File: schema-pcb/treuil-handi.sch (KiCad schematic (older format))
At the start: 7 parts, among them K1 PPM, SW1 calibration, U2 AS5048B Pot, U3 AS5048B moteur

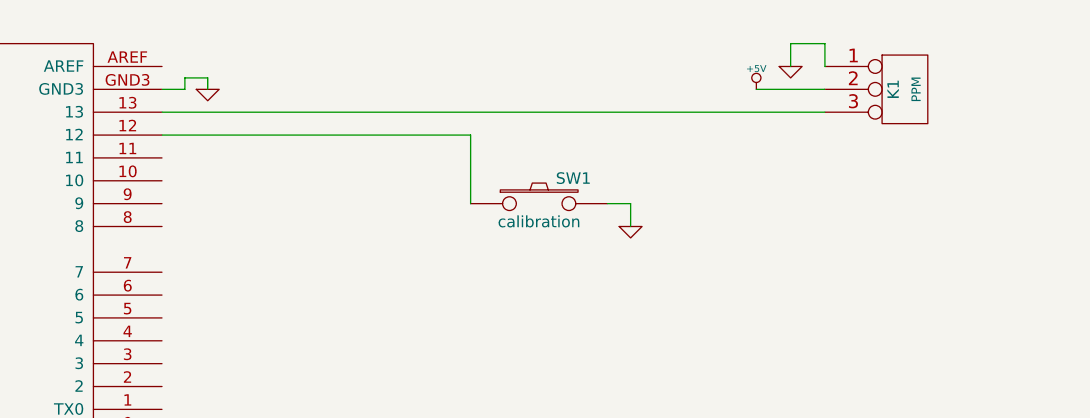
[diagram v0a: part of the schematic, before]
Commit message: maj du schema, doc I2C
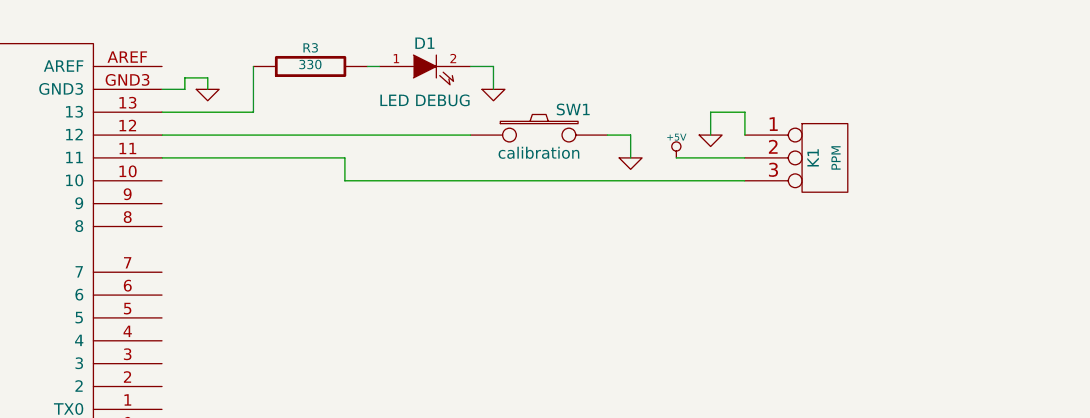
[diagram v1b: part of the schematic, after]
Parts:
- added D1: LED DEBUG, ~, symbol LED
- added R3: 330, ~, symbol R
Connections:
- net GND: now also D1.2 (K)
- net at SHIELD1.11: now also K1.3 (P3)
- net at SHIELD1.13: now also R3.1; no longer K1.3 (P3)
- new net: D1.1 (A), R3.2
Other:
- moved on the sheet: K1, SW1
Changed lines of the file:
@@
-EESchema Schematic File Version 2  date 03/07/2014 16:32:03
+EESchema Schematic File Version 2  date 02/08/2014 10:49:15
 LIBS:power
 LIBS:device
@@
 Sheet 1 1
 Title ""
-Date "3 jul 2014"
+Date "2 aug 2014"
 Rev ""
 Comp ""
@@
 L SW_PUSH SW1
 U 1 1 53B1346F
-P 5200 1900
-F 0 "SW1" H 5350 2010 50  0000 C CNN
-F 1 "calibration" H 5200 1820 50  0000 C CNN
-F 2 "~" H 5200 1900 60  0000 C CNN
-F 3 "~" H 5200 1900 60  0000 C CNN
-	1    5200 1900
+P 5200 1600
+F 0 "SW1" H 5350 1710 50  0000 C CNN
+F 1 "calibration" H 5200 1520 50  0000 C CNN
+F 2 "~" H 5200 1600 60  0000 C CNN
+F 3 "~" H 5200 1600 60  0000 C CNN
+	1    5200 1600
 	1    0    0    -1
 $EndComp
@@
 L GND #PWR06
 U 1 1 53B136FB
-P 5600 2000
-F 0 "#PWR06" H 5600 2000 30  0001 C CNN
-F 1 "GND" H 5600 1930 30  0001 C CNN
-F 2 "" H 5600 2000 60  0000 C CNN
-F 3 "" H 5600 2000 60  0000 C CNN
-	1    5600 2000
-	1    0    0    -1
-$EndComp
-Wire Wire Line
-	5500 1900 5600 1900
-Wire Wire Line
-	5600 1900 5600 2000
+P 5600 1700
+F 0 "#PWR06" H 5600 1700 30  0001 C CNN
+F 1 "GND" H 5600 1630 30  0001 C CNN
+F 2 "" H 5600 1700 60  0000 C CNN
+F 3 "" H 5600 1700 60  0000 C CNN
+	1    5600 1700
+	1    0    0    -1
+$EndComp
+Wire Wire Line
+	5500 1600 5600 1600
+Wire Wire Line
+	5600 1600 5600 1700
 Wire Wire Line
 	7350 3450 7650 3450
@@
 L CONN_3 K1
 U 1 1 53B13AF2
-P 6800 1400
-F 0 "K1" V 6750 1400 50  0000 C CNN
-F 1 "PPM" V 6850 1400 40  0000 C CNN
-F 2 "" H 6800 1400 60  0000 C CNN
-F 3 "" H 6800 1400 60  0000 C CNN
-	1    6800 1400
+P 6450 1700
+F 0 "K1" V 6400 1700 50  0000 C CNN
+F 1 "PPM" V 6500 1700 40  0000 C CNN
+F 2 "" H 6450 1700 60  0000 C CNN
+F 3 "" H 6450 1700 60  0000 C CNN
+	1    6450 1700
 	1    0    0    -1
 $EndComp
@@
 L +5V #PWR?
 U 1 1 53B13B82
-P 6150 1400
-F 0 "#PWR?" H 6150 1490 20  0001 C CNN
-F 1 "+5V" H 6150 1490 30  0000 C CNN
-F 2 "" H 6150 1400 60  0000 C CNN
-F 3 "" H 6150 1400 60  0000 C CNN
-	1    6150 1400
+P 5800 1700
+F 0 "#PWR?" H 5800 1790 20  0001 C CNN
+F 1 "+5V" H 5800 1790 30  0000 C CNN
+F 2 "" H 5800 1700 60  0000 C CNN
+F 3 "" H 5800 1700 60  0000 C CNN
+	1    5800 1700
 	1    0    0    -1
 $EndComp
@@
 L GND #PWR?
 U 1 1 53B13B91
-P 6300 1300
-F 0 "#PWR?" H 6300 1300 30  0001 C CNN
-F 1 "GND" H 6300 1230 30  0001 C CNN
-F 2 "" H 6300 1300 60  0000 C CNN
-F 3 "" H 6300 1300 60  0000 C CNN
-	1    6300 1300
-	1    0    0    -1
-$EndComp
-Wire Wire Line
-	6450 1400 6150 1400
+P 5950 1600
+F 0 "#PWR?" H 5950 1600 30  0001 C CNN
+F 1 "GND" H 5950 1530 30  0001 C CNN
+F 2 "" H 5950 1600 60  0000 C CNN
+F 3 "" H 5950 1600 60  0000 C CNN
+	1    5950 1600
+	1    0    0    -1
+$EndComp
+Wire Wire Line
+	6100 1700 5800 1700
 Wire Wire Line
 	3550 3700 5350 3700
@@
 Connection ~ 5550 3800
 Wire Wire Line
-	6450 1500 3550 1500
-Wire Wire Line
-	6450 1300 6450 1200
-Wire Wire Line
-	6450 1200 6300 1200
-Wire Wire Line
-	6300 1200 6300 1300
+	6100 1600 6100 1500
+Wire Wire Line
+	6100 1500 5950 1500
+Wire Wire Line
+	5950 1500 5950 1600
 Wire Wire Line
 	3550 1400 3650 1400
@@
 Wire Wire Line
 	3550 1600 4900 1600
-Wire Wire Line
-	4900 1600 4900 1900
 $Comp
 L R R1
@@
 	4850 3000 4850 3100
 Connection ~ 4700 3000
+Wire Wire Line
+	6100 1800 4350 1800
+Wire Wire Line
+	4350 1800 4350 1700
+Wire Wire Line
+	4350 1700 3550 1700
+$Comp
+L LED D1
+U 1 1 53DCA5DB
+P 4700 1300
+F 0 "D1" H 4700 1400 50  0000 C CNN
+F 1 "LED DEBUG" H 4700 1150 50  0000 C CNN
+F 2 "~" H 4700 1300 60  0000 C CNN
+F 3 "~" H 4700 1300 60  0000 C CNN
+	1    4700 1300
+	1    0    0    -1
+$EndComp
+$Comp
+L R R3
+U 1 1 53DCA5EA
+P 4200 1300
+F 0 "R3" V 4280 1300 40  0000 C CNN
+F 1 "330" V 4207 1301 40  0000 C CNN
+F 2 "~" V 4130 1300 30  0000 C CNN
+F 3 "~" H 4200 1300 30  0000 C CNN
+	1    4200 1300
+	0    -1   -1   0
+$EndComp
+$Comp
+L GND #PWR?
+U 1 1 53DCA60D
+P 5000 1400
+F 0 "#PWR?" H 5000 1400 30  0001 C CNN
+F 1 "GND" H 5000 1330 30  0001 C CNN
+F 2 "" H 5000 1400 60  0000 C CNN
+F 3 "" H 5000 1400 60  0000 C CNN
+	1    5000 1400
+	1    0    0    -1
+$EndComp
+Wire Wire Line
+	5000 1400 5000 1300
+Wire Wire Line
+	5000 1300 4900 1300
+Wire Wire Line
+	4500 1300 4450 1300
+Wire Wire Line
+	3950 1300 3950 1500
+Wire Wire Line
+	3950 1500 3550 1500
 $EndSCHEMATC
